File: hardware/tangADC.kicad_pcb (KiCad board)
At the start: 2 copper layers, 65.1 x 36.2 mm, 52 parts, among them J1 screw, J2 Conn_01x12_Pin, J3 RJ-2410N, J4 Conn_01x04_Pin, J5 Conn_01x04_Pin, U1 AD9280ARS, U2 Tang_Nano_20K

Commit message: Carrier board v0.2: AIN bias, chip parts, ground vias, edge clearance
Design files only; v0.2 has not been manufactured.  The board as built is
tag v0.1, and hardware/jlcpcb/ still holds v0.1's production files.

- R2 22k -> 10k and a new R19, 47k from AIN to CLAMPIN: AIN gets a DC
  path, and CLAMPIN is 1.0 V instead of 0.625.
- C13 is an 0603 in place of the leaded disc under the module.
- FB1 and FB2 are 0805 chip beads (LCSC C1017, a JLCPCB Basic part).
  The leaded parts doubled as jumpers, so the GND link under FB1 is
  0.6 mm wide there and vias stand where the four holes were.
- GND vias beside U1's ground pins 1, 14 and 16..18.
- The top-edge GND track is 0.69 mm from the edge (was 0.22).
- Silkscreen: revision, Grove 5 V note, J1 polarity, test-point legend.
- Stale no-connect flags in the schematic put right (ERC 14 -> 6).

kicad-cli pcb drc --schematic-parity: nothing unconnected, no parity
error, no clearance error.  docs/pcb-respin.md 4.6 has the details.

Co-Authored-By: Claude Opus 5.5 <noreply@anthropic.com>
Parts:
- added R19: 47k, Resistor_SMD:R_0603_1608Metric, F.Cu at (156.8, 43.7)
- C13: footprint Capacitor_THT:C_Disc_D3.0mm_W2.0mm_P2.50mm -> Capacitor_SMD:C_0603_1608Metric_Pad1.08x0.95mm_HandSolder
- FB1, FB2: value FerriteBead -> 600R@100MHz; footprint Resistor_THT:R_Axial_DIN0204_L3.6mm_D1.6mm_P5.08mm_Horizontal -> Inductor_SMD:L_0805_2012Metric
- R2: value 22k -> 10k
- moved FB2 3.66 mm to (159.6, 34.3)
- moved FB1 2.37 mm to (160.7, 44.0)
- moved C13 1.25 mm to (153.2, 44.2)
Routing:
- net Net-(FB2-Pad1): track 13.3 -> 16.0 mm, vias 0 -> 1
- net Net-(U1-AIN): track 29.7 -> 32.1 mm, vias 0 -> 2
- net +3V3: track 85.8 -> 87.9 mm, vias 4 -> 5
- net +3V3a: track 23.7 -> 25.8 mm, vias 2 -> 3
- net GND: track 278.3 -> 279.6 mm, vias 3 -> 7
- net Net-(U1-CLAMPIN): track 47.4 -> 48.0 mm
- net +3V3d: track 22.7 -> 23.0 mm, vias 0 -> 1
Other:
- board text added: "GND"
- board text added: "Grove:5V"
- board text added: "IN"
- board text added: "TP1 AIN"
- board text added: "TP2 VREF"
- board text added: "TP3 CLAMPIN"
- board text added: "TP4 CLK"
- board text added: "TP5 3V3A"
- board text added: "TP6 3V3D"
- board text added: "TP7 GND"
- board text added: "tangADC v0.2"

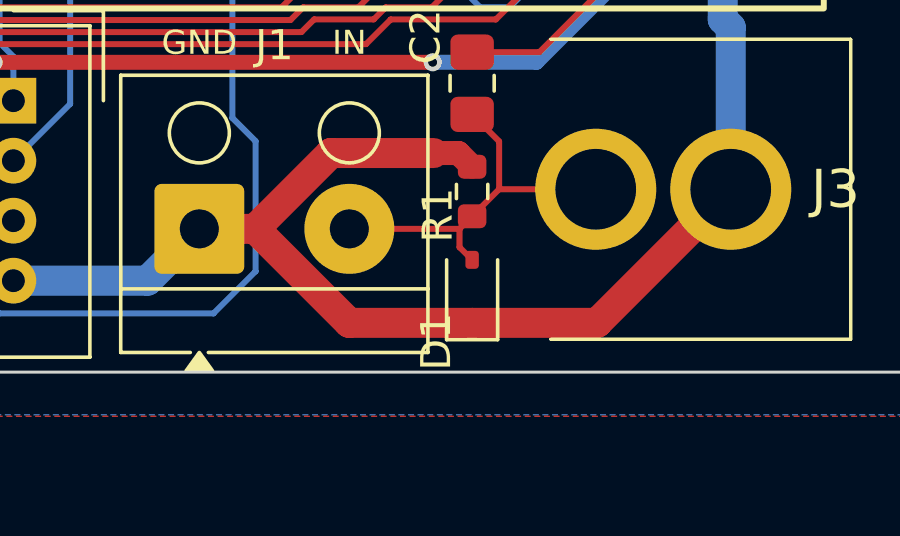
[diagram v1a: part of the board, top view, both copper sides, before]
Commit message: Board v0.2: no Extended parts, and the production files for it
Every part JLCPCB places is now from its Basic or Preferred library
(12 Basic, 1 Preferred); v0.1 had two Extended parts.

- C7: the 1 uF tantalum becomes a 1206 X7R ceramic (C1848) on the same
  pads.
- D1: PESD5V0U1BA in SOD-323 becomes an H5VL10B in DFN1006-2L
  (C7420372, footprint D_SOD-882), still bidirectional.  No fee-free
  bidirectional ESD part exists in SOD-323.
- BOM, CPL and Gerbers regenerated for v0.2, in the JLCPCB-tools
  plugin's layout; its project.db carries the same LCSC numbers.

The Gerbers come from kicad-cli.  The same commands run on the v0.1
board reproduce seven of the nine ordered layers and both drill files
byte for byte apart from the date; the other two differ by one pour
vertex and by the mask openings of the four mounting holes.

kicad-cli pcb drc --schematic-parity: nothing unconnected, no parity
error, no clearance error.  docs/pcb-respin.md 4.7 has the details.

Co-Authored-By: Claude Opus 5.5 <noreply@anthropic.com>
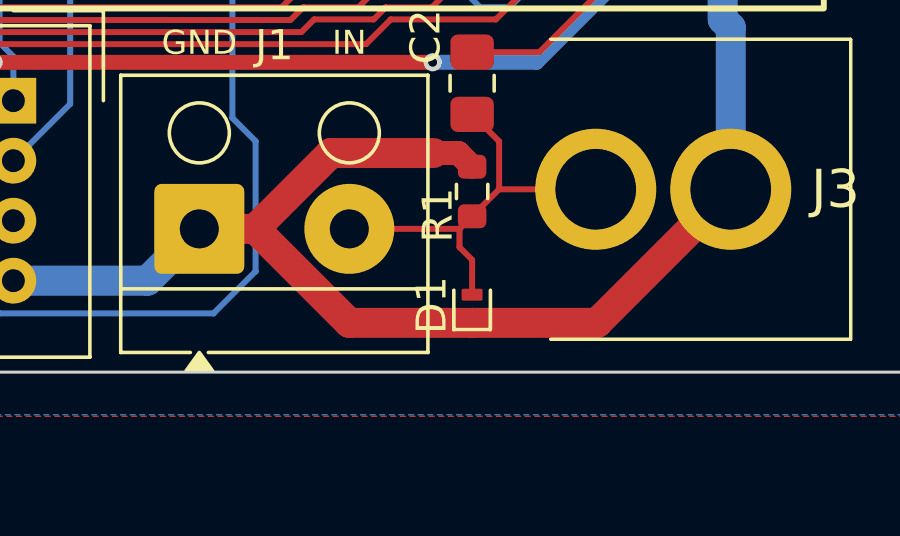
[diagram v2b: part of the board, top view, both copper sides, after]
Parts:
- D1: value PESD5V0U1BA -> H5VL10B; footprint Diode_SMD:D_SOD-323 -> Diode_SMD:D_SOD-882
- moved D1 0.46 mm to (149.2, 60.0)
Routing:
- net Net-(D1-A2): track 12.8 -> 14.0 mm
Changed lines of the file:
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@@
 		(sheetname "/")
 		(sheetfile "tangADC.kicad_sch")
+		(units
+			(unit
+				(name "A")
+				(pins "1" "2")
+			)
+		)
 		(attr smd)
 		(duplicate_pad_numbers_are_jumpers no)
@@
 		)
 	)
-	(footprint "Diode_SMD:D_SOD-323"
+	(footprint "Diode_SMD:D_SOD-882"
 		(layer "F.Cu")
-		(at 149.178 59.5884 90)
-		(descr "SOD-323")
-		(tags "SOD-323")
+		(at 149.178 60.05 90)
+		(descr "SOD-882, DFN1006-2, body 1.0 x 0.6 x 0.48mm, pitch 0.65mm, https://assets.nexperia.com/documents/package-information/SOD882.pdf")
+		(tags "Diode SOD882 DFN1006-2")
 		(property "Reference" "D1"
-			(at -1.6764 -1.1976 90)
+			(at 0 -1.35 90)
 			(layer "F.SilkS")
 			(effects
@@
 			)
 		)
-		(property "Value" "PESD5V0U1BA"
-			(at -3.6576 3.9332 180)
+		(property "Value" "H5VL10B"
+			(at 0 1.35 90)
 			(layer "F.Fab")
 			(effects
@@
 			)
 		)
-		(property "LCSC" "C5199862"
-			(at 0 0 0)
-			(layer "F.SilkS")
-			(hide yes)
-			(effects
-				(font
-					(size 1.27 1.27)
-					(thickness 0.15)
-				)
-			)
-		)
 		(property ki_fp_filters "TO-???* *_Diode_* *SingleDiode* D_*")
 		(sheetname "/")
 		(sheetfile "tangADC.kicad_sch")
-		(units
-			(unit
-				(name "A")
-				(pins "1" "2")
-			)
-		)
 		(attr smd)
 		(duplicate_pad_numbers_are_jumpers no)
 		(fp_line
-			(start -1.61 -0.85)
-			(end 1.05 -0.85)
+			(start -0.81 -0.61)
+			(end 0.5 -0.61)
 			(stroke
 				(width 0.12)
@@
 		)
 		(fp_line
-			(start -1.61 -0.85)
-			(end -1.61 0.85)
+			(start -0.81 -0.61)
+			(end -0.81 0.61)
 			(stroke
 				(width 0.12)
@@
 		)
 		(fp_line
-			(start -1.61 0.85)
-			(end 1.05 0.85)
+			(start -0.81 0.61)
+			(end 0.5 0.61)
 			(stroke
 				(width 0.12)
@@
 		)
 		(fp_line
-			(start 1.6 -0.95)
-			(end 1.6 0.95)
+			(start 0.8 -0.6)
+			(end 0.8 0.6)
 			(stroke
 				(width 0.05)
@@
 		)
 		(fp_line
-			(start -1.6 -0.95)
-			(end 1.6 -0.95)
+			(start -0.8 -0.6)
+			(end 0.8 -0.6)
 			(stroke
 				(width 0.05)
@@
 		)
 		(fp_line
-			(start -1.6 -0.95)
-			(end -1.6 0.95)
+			(start -0.8 -0.6)
+			(end -0.8 0.6)
 			(stroke
 				(width 0.05)
@@
 		)
 		(fp_line
-			(start -1.6 0.95)
-			(end 1.6 0.95)
+			(start 0.8 0.6)
+			(end -0.8 0.6)
 			(stroke
 				(width 0.05)
@@
 		)
 		(fp_line
-			(start 0.9 -0.7)
-			(end 0.9 0.7)
+			(start 0.5 -0.3)
+			(end 0.5 0.3)
 			(stroke
 				(width 0.1)
@@
 		)
 		(fp_line
-			(start -0.9 -0.7)
-			(end 0.9 -0.7)
+			(start -0.5 -0.3)
+			(end 0.5 -0.3)
 			(stroke
 				(width 0.1)
@@
 		)
 		(fp_line
-			(start 0.2 -0.35)
-			(end 0.2 0.35)
+			(start 0.15 -0.2)
+			(end -0.15 0)
 			(stroke
 				(width 0.1)
@@
 		)
 		(fp_line
-			(start -0.3 -0.35)
-			(end -0.3 0.35)
+			(start 0.15 0)
+			(end 0.3 0)
 			(stroke
 				(width 0.1)
@@
 		)
 		(fp_line
-			(start 0.2 0)
-			(end 0.45 0)
+			(start -0.15 0)
+			(end -0.3 0)
 			(stroke
 				(width 0.1)
@@
 		)
 		(fp_line
-			(start -0.3 0)
-			(end 0.2 -0.35)
+			(start -0.15 0)
+			(end 0.15 0.2)
 			(stroke
 				(width 0.1)
@@
 		)
 		(fp_line
-			(start -0.3 0)
-			(end -0.5 0)
+			(start 0.15 0.2)
+			(end 0.15 -0.2)
 			(stroke
 				(width 0.1)
@@
 		)
 		(fp_line
-			(start 0.2 0.35)
-			(end -0.3 0)
+			(start -0.15 0.2)
+			(end -0.15 -0.2)
 			(stroke
 				(width 0.1)
@@
 		)
 		(fp_line
-			(start 0.9 0.7)
-			(end -0.9 0.7)
+			(start 0.5 0.3)
+			(end -0.5 0.3)
 			(stroke
 				(width 0.1)
@@
 		)
 		(fp_line
-			(start -0.9 0.7)
-			(end -0.9 -0.7)
+			(start -0.5 0.3)
+			(end -0.5 -0.3)
 			(stroke
 				(width 0.1)
@@
 		)
 		(fp_text user "${REFERENCE}"
-			(at -1.6764 -1.1976 90)
+			(at -0.127 -1.35 90)
 			(layer "F.Fab")
 			(effects
@@
 			)
 		)
+		(pad "" smd roundrect
+			(at -0.35 0 90)
+			(size 0.3 0.6)
+			(layers "F.Paste")
+			(roundrect_rratio 0.1666666667)
+			(solder_paste_margin -0.05)
+		)
+		(pad "" smd roundrect
+			(at 0.35 0 90)
+			(size 0.3 0.6)
+			(layers "F.Paste")
+			(roundrect_rratio 0.1666666667)
+			(solder_paste_margin -0.05)
+		)
 		(pad "1" smd roundrect
-			(at -1.05 0 90)
-			(size 0.6 0.45)
-			(layers "F.Cu" "F.Mask" "F.Paste")
-			(roundrect_rratio 0.25)
+			(at -0.35 0 90)
+			(size 0.4 0.7)
+			(layers "F.Cu" "F.Mask")
+			(roundrect_rratio 0.125)
 			(net "GND")
 			(pinfunction "A1_1")
 			(pintype "passive")
+			(solder_paste_margin -0.05)
 		)
 		(pad "2" smd roundrect
-			(at 1.05 0 90)
-			(size 0.6 0.45)
-			(layers "F.Cu" "F.Mask" "F.Paste")
-			(roundrect_rratio 0.25)
+			(at 0.35 0 90)
+			(size 0.4 0.7)
+			(layers "F.Cu" "F.Mask")
+			(roundrect_rratio 0.125)
 			(net "Net-(D1-A2)")
 			(pinfunction "A2_2")
 			(pintype "passive")
+			(solder_paste_margin -0.05)
 		)
 		(embedded_fonts no)
-		(model "${KICAD10_3DMODEL_DIR}/Diode_SMD.3dshapes/D_SOD-323.step"
+		(model "${KICAD10_3DMODEL_DIR}/Diode_SMD.3dshapes/D_SOD-882.step"
 			(offset
 				(xyz 0 0 0)
@@
 		(sheetname "/")
 		(sheetfile "tangADC.kicad_sch")
+		(units
+			(unit
+				(name "A")
+				(pins "1" "2")
+			)
+		)
 		(attr smd)
 		(duplicate_pad_numbers_are_jumpers no)
@@
 		(width 0.2)
 		(layer "F.Cu")
+		(net "Net-(D1-A2)")
+	)
+	(segment
+		(start 149.178 58.5384)
+		(end 149.178 59.7)
+		(width 0.2)
+		(layer "F.Cu")
